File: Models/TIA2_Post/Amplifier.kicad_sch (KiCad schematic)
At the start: 0 parts

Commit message: Save progress
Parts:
- added C1, C2: 100 nF, 0603, symbol Device:C
- added U1: OP37G, IC:PDIP-8, symbol Vendor:OP37G
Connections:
- new net -15V: C2.1, U1.4 (V-)
- new net 15V: C1.1, U1.7 (V+)
- new net GND: C1.2, C2.2
- no-connect marks 0 -> 3

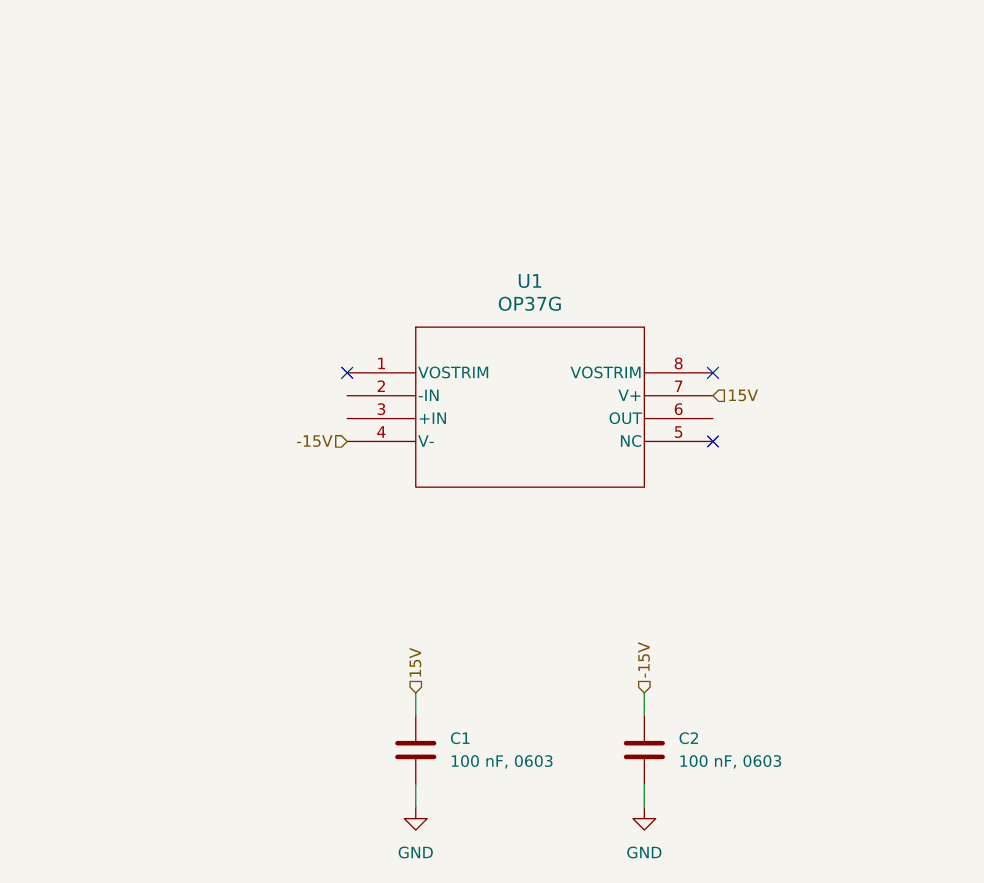
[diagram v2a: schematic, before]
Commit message: Finished with the chips for the transimpedance amplifiers
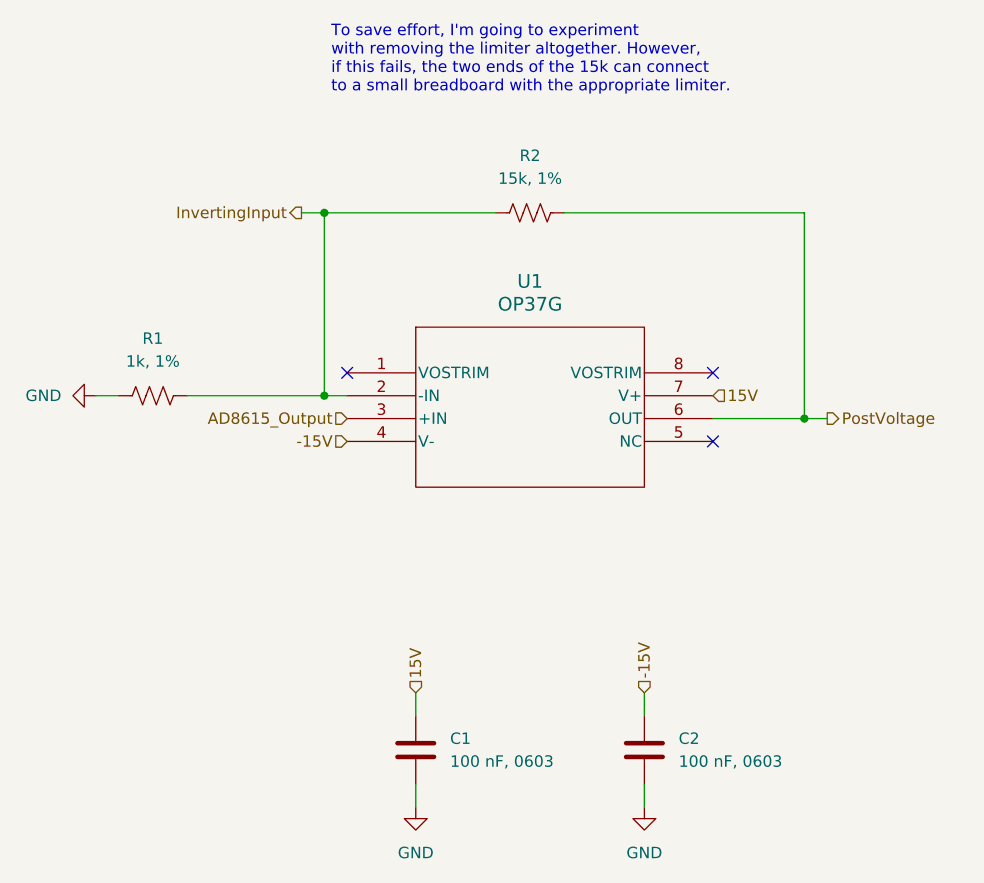
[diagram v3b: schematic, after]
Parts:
- added R1: 1k, 1%, symbol Device:R_US
- added R2: 15k, 1%, symbol Device:R_US
- U1: now in the parts list
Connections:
- net GND: now also R1.1
- net InvertingInput: now reaches U1.2 (-IN)
- net InvertingInput: now also R1.2, R2.1
- net AD8615_Output: now reaches U1.3 (+IN)
- net PostVoltage: now reaches U1.6 (OUT)
- net PostVoltage: now also R2.2
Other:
- note added: "To save effort, I'm going to experiment with removing the limiter altogether. However, if this fails, the two ends of the 15k can connect to a small breadboard with the appropriate limiter."

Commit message: Save progress
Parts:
- removed R1: 1k, 1%, symbol Device:R_US
- removed R2: 15k, 1%, symbol Device:R_US
- removed U1: OP37G, IC:PDIP-8, symbol Vendor:OP37G
- added R10: 1k, 1%, symbol Device:R_US
- added R9: 15k, 1%, symbol Device:R_US
- added U2: OP37G, symbol Amplifier_Operational:OP07
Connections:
- net -15V: now also U2.4 (V-)
- net 15V: now also U2.7 (V+)
- net AD8615_Output: now also U2.3 (+)
- net GND: now also R10.1
- net InvertingInput: now also R10.2, R9.1, U2.2 (-)
- net PostVoltage: now also R9.2, U2.6
- no-connect marks 3 -> 2
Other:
- note removed: "To save effort, I'm going to experiment with removing the limiter altogether. However, if this fails, the two ends of the 15k can connect to a small breadboard with the appropriate limiter."

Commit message: Save progress
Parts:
- removed U2: OP37G, symbol Amplifier_Operational:OP07
- added U1: OP37G, IC:SOIC-8, symbol Amplifier_Operational:OP07
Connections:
- net -15V: now also U1.4 (V-)
- net 15V: now also U1.7 (V+)
- net AD8615_Output: now also U1.3 (+)
- net InvertingInput: now also U1.2 (-)
- net PostVoltage: now also U1.6
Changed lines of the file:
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@@
-	)
-	(symbol
-		(lib_id "Amplifier_Operational:OP07")
-		(at 116.84 76.2 0)
-		(unit 1)
-		(exclude_from_sim no)
-		(in_bom yes)
-		(on_board yes)
-		(dnp no)
-		(fields_autoplaced yes)
-		(property "Reference" "U2"
-			(at 125.73 69.7798 0)
-			(effects
-				(font
-					(size 1.27 1.27)
-				)
-			)
-		)
-		(property "Value" "OP37G"
-			(at 125.73 72.3198 0)
-			(effects
-				(font
-					(size 1.27 1.27)
-				)
-			)
-		)
-		(property "Footprint" ""
-			(at 118.11 74.93 0)
-			(effects
-				(font
-					(size 1.27 1.27)
-				)
-				(hide yes)
-			)
-		)
-		(property "Datasheet" ""
-			(at 118.11 72.39 0)
-			(effects
-				(font
-					(size 1.27 1.27)
-				)
-				(hide yes)
-			)
-		)
-		(property "Description" ""
-			(at 116.84 76.2 0)
-			(effects
-				(font
-					(size 1.27 1.27)
-				)
-				(hide yes)
-			)
-		)
-		(property "Purchase Link" "https://www.mouser.com/ProductDetail/Analog-Devices/OP37GPZ?qs=WIvQP4zGaniU2Gv%2FvPojWw%3D%3D"
-			(at 116.84 76.2 0)
-			(effects
-				(font
-					(size 1.27 1.27)
-				)
-				(hide yes)
-			)
-		)
-		(pin "3"
-		)
-		(pin "2"
-		)
-		(pin "6"
-		)
-		(pin "4"
-		)
-		(pin "7"
-		)
-		(pin "1"
-		)
-		(pin "5"
-		)
-		(pin "8"
-		)
-		(instances
-			(project ""
-				(path "/f19129fc-f916-4692-924c-ee308c6b3e1d/576e9362-b988-409f-82c5-0c80cb18568a"
-					(reference "U2")
-					(unit 1)
-				)
-			)
-		)
 	)
 	(symbol
@@
 					(unit 1)
 				)
+			)
+		)
+	)
+	(symbol
+		(lib_name "OP07_1")
+		(lib_id "Amplifier_Operational:OP07")
+		(at 116.84 76.2 0)
+		(unit 1)
+		(exclude_from_sim no)
+		(in_bom yes)
+		(on_board yes)
+		(dnp no)
+		(fields_autoplaced yes)
+		(property "Reference" "U1"
+			(at 125.73 69.7798 0)
+			(effects
+				(font
+					(size 1.27 1.27)
+				)
+			)
+		)
+		(property "Value" "OP37G"
+			(at 125.73 72.3198 0)
+			(effects
+				(font
+					(size 1.27 1.27)
+				)
+			)
+		)
+		(property "Footprint" "IC:SOIC-8"
+			(at 118.11 74.93 0)
+			(effects
+				(font
+					(size 1.27 1.27)
+				)
+				(hide yes)
+			)
+		)
+		(property "Datasheet" ""
+			(at 118.11 72.39 0)
+			(effects
+				(font
+					(size 1.27 1.27)
+				)
+				(hide yes)
+			)
+		)
+		(property "Description" ""
+			(at 116.84 76.2 0)
+			(effects
+				(font
+					(size 1.27 1.27)
+				)
+				(hide yes)
+			)
+		)
+		(property "Purchase Link" "https://www.mouser.com/ProductDetail/Analog-Devices/OP37GSZ-REEL7?qs=WIvQP4zGanjNS2P5vdTsvA%3D%3D"
+			(at 116.84 76.2 0)
+			(effects
+				(font
+					(size 1.27 1.27)
+				)
+				(hide yes)
+			)
+		)
+		(pin "8"
+		)
+		(pin "4"
+		)
+		(pin "6"
+		)
+		(pin "1"
+		)
+		(pin "5"
+		)
+		(pin "2"
+		)
+		(pin "7"
+		)
+		(pin "3"
+		)
+		(instances
+			(project ""
+				(path "/f19129fc-f916-4692-924c-ee308c6b3e1d/576e9362-b988-409f-82c5-0c80cb18568a"
+					(reference "U1")
+					(unit 1)
+				)

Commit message: Save progress
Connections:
- net GND: no longer R10.1
- new net ISO_GND: R10.1
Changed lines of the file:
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@@
+		)
+	)
+	(global_label "-15V"
+		(shape input)
+		(at 114.3 83.82 270)
+		(fields_autoplaced yes)
+		(effects
+			(font
+				(size 1.27 1.27)
+			)
+			(justify right)
+		)
+		(property "Intersheetrefs" "${INTERSHEET_REFS}"
+			(at 114.3 91.8852 90)
+			(effects
+				(font
+					(size 1.27 1.27)
+				)
+				(justify right)
+				(hide yes)
+			)
+		)
+	)
+	(global_label "15V"
+		(shape input)
+		(at 114.3 68.58 90)
+		(fields_autoplaced yes)
+		(effects
+			(font
+				(size 1.27 1.27)
+			)
+			(justify left)
+		)
+		(property "Intersheetrefs" "${INTERSHEET_REFS}"
+			(at 114.3 62.0872 90)
+			(effects
+				(font
+					(size 1.27 1.27)
+				)
+				(justify left)
+				(hide yes)
+			)
+		)
+	)
+	(global_label "ISO_GND"
+		(shape bidirectional)
+		(at 91.44 101.6 180)
+		(fields_autoplaced yes)
+		(effects
+			(font
+				(size 1.27 1.27)
+			)
+			(justify right)
+		)
+		(property "Intersheetrefs" "${INTERSHEET_REFS}"
+			(at 79.3606 101.6 0)
+			(effects
+				(font
+					(size 1.27 1.27)
+				)
+				(justify right)
+				(hide yes)
+			)
+		)
+	)
+	(global_label "15V"
+		(shape input)
+		(at 101.6 116.84 90)
+		(fields_autoplaced yes)
+		(effects
+			(font
+				(size 1.27 1.27)
+			)
+			(justify left)
+		)
+		(property "Intersheetrefs" "${INTERSHEET_REFS}"
+			(at 101.6 110.3472 90)
+			(effects
+				(font
+					(size 1.27 1.27)
+				)
+				(justify left)
+				(hide yes)
+			)
+		)
+	)
+	(global_label "-15V"
+		(shape input)
+		(at 127 116.84 90)
+		(fields_autoplaced yes)
+		(effects
+			(font
+				(size 1.27 1.27)
+			)
+			(justify left)
+		)
+		(property "Intersheetrefs" "${INTERSHEET_REFS}"
+			(at 127 108.7748 90)
+			(effects
+				(font
+					(size 1.27 1.27)
+				)
+				(justify left)
+				(hide yes)
+			)
 		)
 	)
@@
 		)
 	)
-	(hierarchical_label "-15V"
-		(shape input)
-		(at 127 116.84 90)
-		(effects
-			(font
-				(size 1.27 1.27)
-			)
-			(justify left)
-		)
-	)
 	(hierarchical_label "InvertingInput"
 		(shape input)
@@
 			)
 			(justify right)
-		)
-	)
-	(hierarchical_label "15V"
-		(shape input)
-		(at 114.3 68.58 90)
-		(effects
-			(font
-				(size 1.27 1.27)
-			)
-			(justify left)
-		)
-	)
-	(hierarchical_label "-15V"
-		(shape input)
-		(at 114.3 83.82 270)
-		(effects
-			(font
-				(size 1.27 1.27)
-			)
-			(justify right)
-		)
-	)
-	(hierarchical_label "15V"
-		(shape input)
-		(at 101.6 116.84 90)
-		(effects
-			(font
-				(size 1.27 1.27)
-			)
-			(justify left)
 		)
 	)
@@
 					(unit 1)
 				)
-			)
-		)
-	)
-	(symbol
-		(lib_id "power:GND")
-		(at 91.44 101.6 270)
-		(unit 1)
-		(exclude_from_sim no)
-		(in_bom yes)
-		(on_board yes)
-		(dnp no)
-		(fields_autoplaced yes)
-		(property "Reference" "#PWR06"
-			(at 85.09 101.6 0)
-			(effects
-				(font
-					(size 1.27 1.27)
-				)
-				(hide yes)
-			)
-		)
-		(property "Value" "GND"
-			(at 87.63 101.5999 90)
-			(effects
-				(font
-					(size 1.27 1.27)
-				)
-				(justify right)
-			)
-		)
-		(property "Footprint" ""
-			(at 91.44 101.6 0)
-			(effects
-				(font
-					(size 1.27 1.27)
-				)
-				(hide yes)
-			)
-		)
-		(property "Datasheet" ""
-			(at 91.44 101.6 0)
-			(effects
-				(font
-					(size 1.27 1.27)
-				)
-				(hide yes)
-			)
-		)
-		(property "Description" "Power symbol creates a global label with name \"GND\" , ground"
-			(at 91.44 101.6 0)
-			(effects
-				(font
-					(size 1.27 1.27)
-				)
-				(hide yes)
-			)
-		)
-		(pin "1"
-		)
-		(instances
-			(project "TIA2_Post"
-				(path "/f19129fc-f916-4692-924c-ee308c6b3e1d/576e9362-b988-409f-82c5-0c80cb18568a"
-					(reference "#PWR06")
-					(unit 1)
-				)

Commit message: Save progress
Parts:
- R9: value 15k, 1% -> 24k, 1%; Purchase Link (none) -> https://www.digikey.com/en/products/detail/vishay-dale/CRCW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
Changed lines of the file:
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@@
 			)
 		)
-		(property "Value" "15k, 1%"
+		(property "Value" "24k, 1%"
 			(at 115.57 97.79 90)
 			(effects
@@
 			(at 115.57 101.6 0)
 			(effects
+				(font
+					(size 1.27 1.27)
+				)
+				(hide yes)
+			)
+		)
+		(property "Purchase Link" "https://www.digikey.com/en/products/detail/vishay-dale/CRCW060324K0FKEA/1174823"
+			(at 115.57 101.6 0)
+			(effects

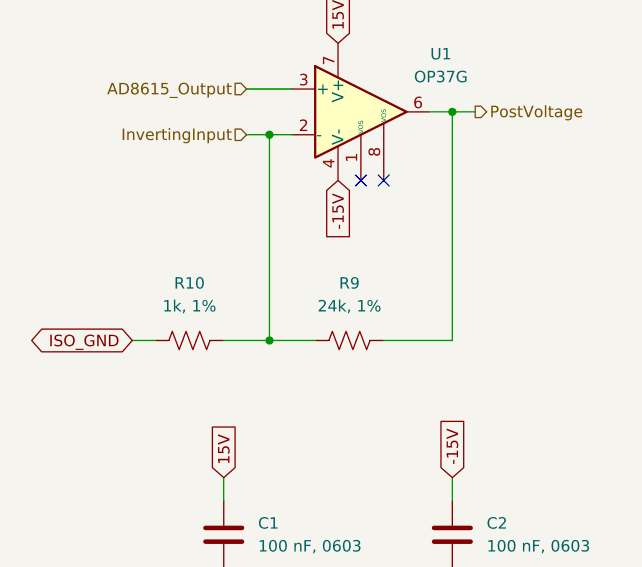
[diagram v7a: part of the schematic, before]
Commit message: ERC passes for the two new boards
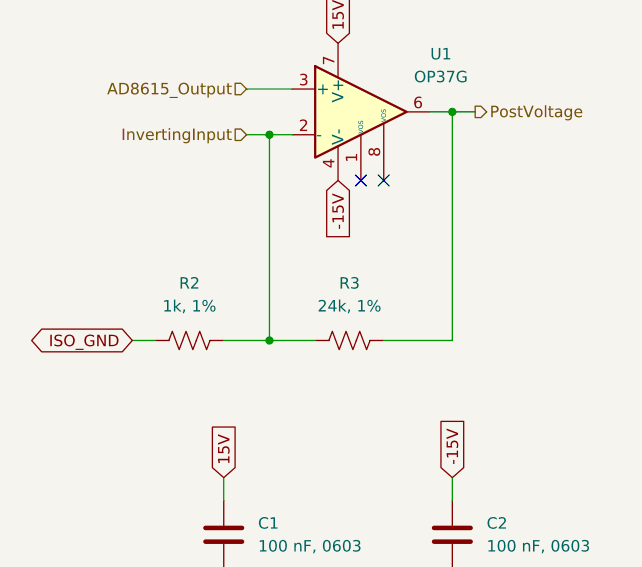
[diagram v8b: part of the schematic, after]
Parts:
- C1, C2: footprint (none) -> TwoTerminal:CAPC0603; Cost (none) -> $0.079; Purchase Link (none) -> https://www.digikey.com/en/products/detail/murata-electroni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
- R2: renamed from R10; footprint (none) -> TwoTerminal:RESC0603; Cost (none) -> $0.030; Purchase Link (none) -> https://www.digikey.com/en/products/detail/vishay-dale/CRCW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
- R3: renamed from R9; footprint (none) -> TwoTerminal:RESC0603; Cost (none) -> $0.030
- U1: Cost (none) -> $5.770
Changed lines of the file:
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@@
 			)
 		)
-		(property "Footprint" ""
+		(property "Footprint" "TwoTerminal:CAPC0603"
 			(at 102.5652 127 0)
 			(effects
@@
 			)
 		)
-		(property "Purchase Link" ""
+		(property "Purchase Link" "https://www.digikey.com/en/products/detail/murata-electronics/GRM188R72A104KA35D/702549"
+			(at 101.6 123.19 0)
+			(effects
+				(font
+					(size 1.27 1.27)
+				)
+				(hide yes)
+			)
+		)
+		(property "Cost" "$0.079"
 			(at 101.6 123.19 0)
 			(effects
@@
 		(dnp no)
 		(fields_autoplaced yes)
-		(property "Reference" "#PWR02"
+		(property "Reference" "#PWR05"
 			(at 101.6 135.89 0)
 			(effects
@@
 			(project ""
 				(path "/f19129fc-f916-4692-924c-ee308c6b3e1d/576e9362-b988-409f-82c5-0c80cb18568a"
-					(reference "#PWR02")
+					(reference "#PWR05")
 					(unit 1)
 				)
@@
 		(dnp no)
 		(fields_autoplaced yes)
-		(property "Reference" "R10"
+		(property "Reference" "R2"
 			(at 97.79 95.25 90)
 			(effects
@@
 			)
 		)
-		(property "Footprint" ""
+		(property "Footprint" "TwoTerminal:RESC0603"
 			(at 98.044 100.584 90)
 			(effects
@@
 			)
 		)
-		(property "Purchase Link" ""
+		(property "Purchase Link" "https://www.digikey.com/en/products/detail/vishay-dale/CRCW06031K00FKEA/1174668"
 			(at 97.79 101.6 0)
+			(effects
+				(font
+					(size 1.27 1.27)
+				)
+				(hide yes)
+			)
+		)
+		(property "Cost" "$0.030"
+			(at 97.79 101.6 90)
 			(effects
 				(font
@@
 			(project "TIA2_Post"
 				(path "/f19129fc-f916-4692-924c-ee308c6b3e1d/576e9362-b988-409f-82c5-0c80cb18568a"
-					(reference "R10")
+					(reference "R2")
 					(unit 1)
 				)
@@
 		(dnp no)
 		(fields_autoplaced yes)
-		(property "Reference" "R9"
+		(property "Reference" "R3"
 			(at 115.57 95.25 90)
 			(effects
@@
 			)
 		)
-		(property "Footprint" ""
+		(property "Footprint" "TwoTerminal:RESC0603"
 			(at 115.824 100.584 90)
 			(effects
@@
 		(property "Purchase Link" "https://www.digikey.com/en/products/detail/vishay-dale/CRCW060324K0FKEA/1174823"
 			(at 115.57 101.6 0)
+			(effects
+				(font
+					(size 1.27 1.27)
+				)
+				(hide yes)
+			)
+		)
+		(property "Cost" "$0.030"
+			(at 115.57 101.6 90)
 			(effects
 				(font
@@
 			(project "TIA2_Post"
 				(path "/f19129fc-f916-4692-924c-ee308c6b3e1d/576e9362-b988-409f-82c5-0c80cb18568a"
-					(reference "R9")
+					(reference "R3")
 					(unit 1)
 				)
@@
 			)
 		)
+		(property "Cost" "$5.770"
+			(at 116.84 76.2 0)
+			(effects
+				(font
+					(size 1.27 1.27)
+				)
+				(hide yes)
+			)
+		)
 		(pin "8"
 		)
@@
 		(dnp no)
 		(fields_autoplaced yes)
-		(property "Reference" "#PWR03"
+		(property "Reference" "#PWR06"
 			(at 127 135.89 0)
 			(effects
@@
 			(project "TIA2_Post"
 				(path "/f19129fc-f916-4692-924c-ee308c6b3e1d/576e9362-b988-409f-82c5-0c80cb18568a"
-					(reference "#PWR03")
+					(reference "#PWR06")
 					(unit 1)
 				)
@@
 			)
 		)
-		(property "Footprint" ""
+		(property "Footprint" "TwoTerminal:CAPC0603"
 			(at 127.9652 127 0)
 			(effects
@@
 			)
 		)
-		(property "Purchase Link" ""
+		(property "Purchase Link" "https://www.digikey.com/en/products/detail/murata-electronics/GRM188R72A104KA35D/702549"
 			(at 127 123.19 0)
 			(effects
+				(font
+					(size 1.27 1.27)
+				)
+				(hide yes)
+			)
+		)
+		(property "Cost" "$0.079"
+			(at 127 123.19 0)
+			(effects
